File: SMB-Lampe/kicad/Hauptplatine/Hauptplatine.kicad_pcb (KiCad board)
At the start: 2 copper layers, 2 parts, among them J1 Screw_Terminal_01x03, U1 MOUDLE-SEEEDUINO-XIAO-ESP32C3

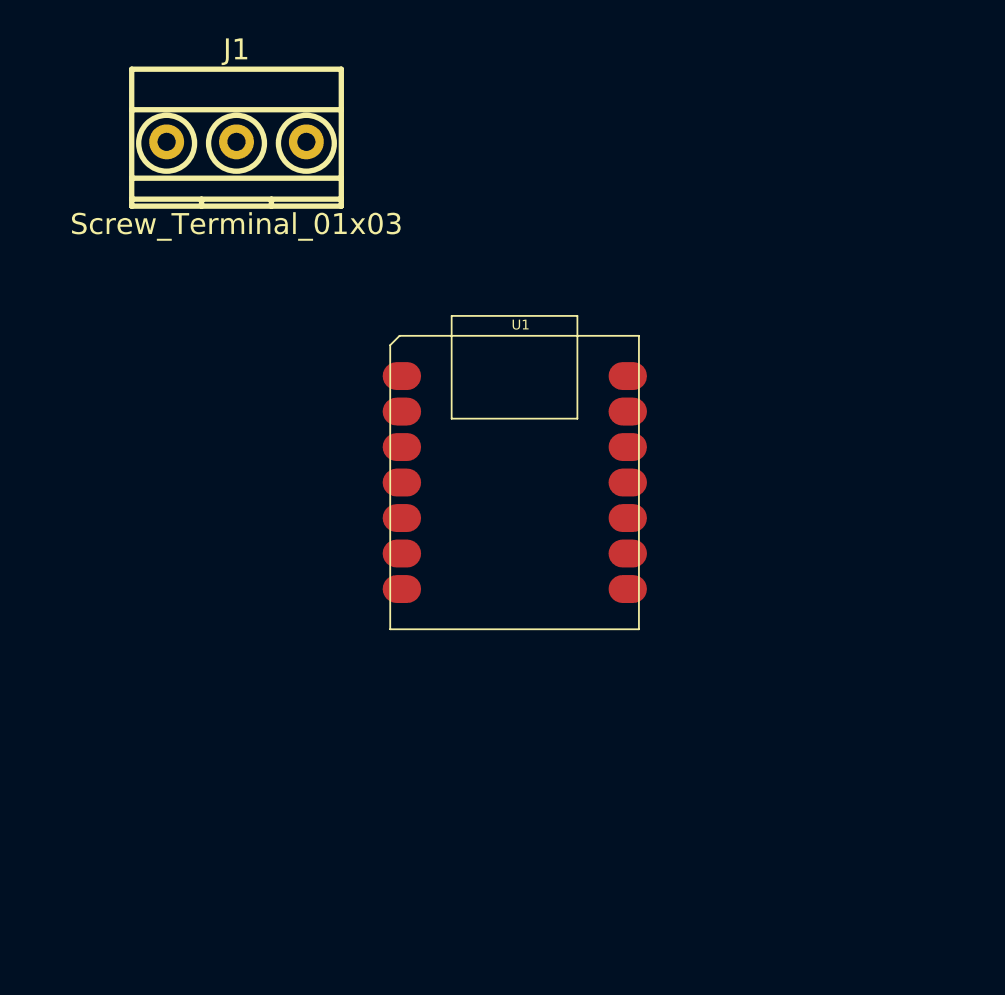
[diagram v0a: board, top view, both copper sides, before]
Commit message: Hauptplatine fertig
Hauptplatine mit ESP Levelshifter und Screwsockets
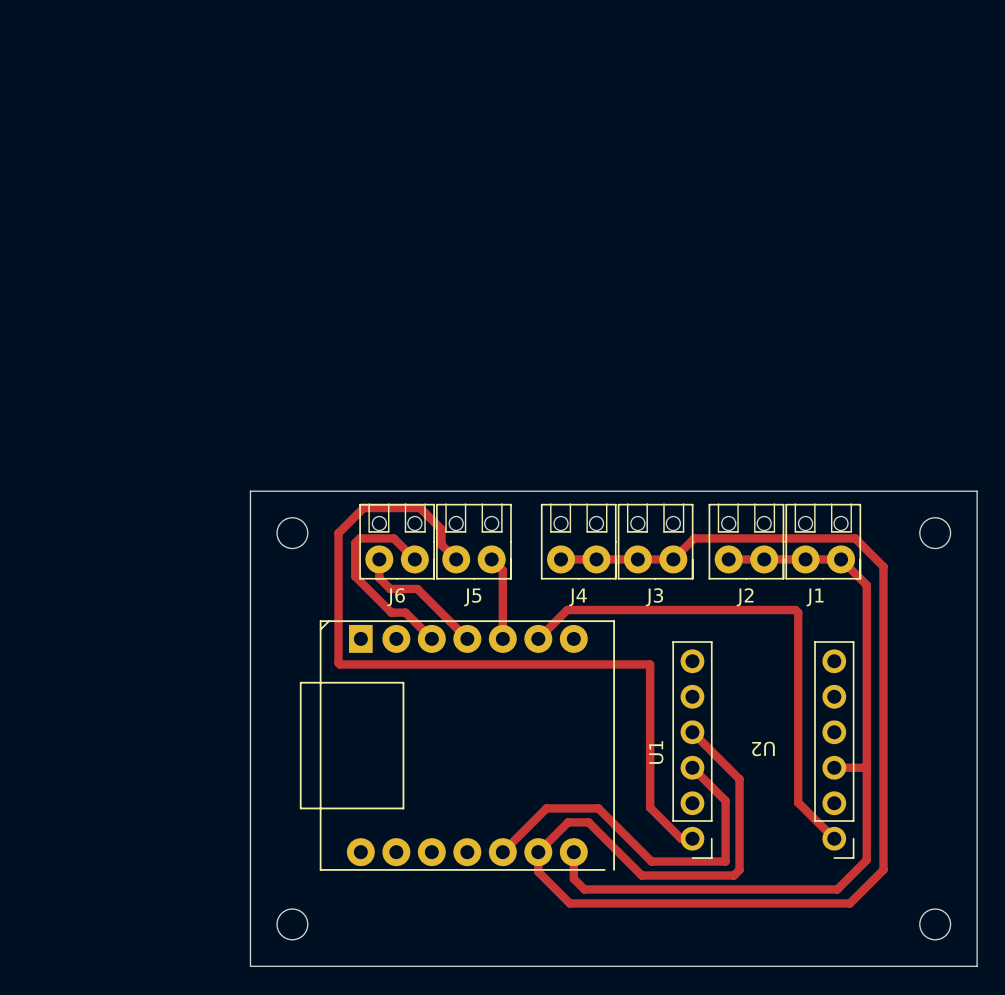
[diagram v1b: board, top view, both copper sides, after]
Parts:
- added J2: Screw_Terminal_01x02, Eigenen_Library:Screw Terminal, F.Cu at (141.5, 79.9)
- added J3: Screw_Terminal_01x02, Eigenen_Library:Screw Terminal, F.Cu at (135.0, 79.9)
- added J4: Screw_Terminal_01x02, Eigenen_Library:Screw Terminal, F.Cu at (129.5, 79.9)
- added J5: Screw_Terminal_01x02, Eigenen_Library:Screw Terminal, F.Cu at (122.0, 79.9)
- added J6: Screw_Terminal_01x02, Eigenen_Library:Screw Terminal, F.Cu at (116.5, 79.9)
- added REF**: MountingHole_2.2mm_M2_DIN965, MountingHole:MountingHole_2.2mm_M2_DIN965, F.Cu at (155.0, 110.0)
- added REF**: MountingHole_2.2mm_M2_DIN965, MountingHole:MountingHole_2.2mm_M2_DIN965, F.Cu at (155.0, 82.0)
- added REF**: MountingHole_2.2mm_M2_DIN965, MountingHole:MountingHole_2.2mm_M2_DIN965, F.Cu at (109.0, 110.0)
- added REF**: MountingHole_2.2mm_M2_DIN965, MountingHole:MountingHole_2.2mm_M2_DIN965, F.Cu at (109.0, 82.0)
- added U2: 4-Kanal-I2C Pegelwandler, Eigenen_Library:I2C Levelshifter, F.Cu at (142.8, 89.4)
- J1: value Screw_Terminal_01x03 -> Screw_Terminal_01x02; footprint w_conn_mkds:mkds_1,5-3 -> Eigenen_Library:Screw Terminal
- U1: footprint xiao ESP32C3_PCB:MOUDLE14P-SMD-2.54-21X17.8MM -> Eigenen_Library:ESP32 C3
- moved J1 49.3 mm to (147.0, 79.9), turned to 180 degrees
- moved U1 18.1 mm to (132.0, 97.2), turned to 90 degrees
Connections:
- J1 pad 1: unconnected-(J1-Pin_1-Pad1) -> +5V
- J1 pad 2: unconnected-(J1-Pin_2-Pad2) -> +5V
- U1 pad 12: unconnected-(U1-3V3-Pad12) -> +3.3V
- U1 pad 13: unconnected-(U1-GND-Pad13) -> GND
- U1 pad 14: unconnected-(U1-5V-Pad14) -> +5V
- U1 pad 3: unconnected-(U1-PA10_A2_D2-Pad3) -> Steuer_Servo
- U1 pad 4: unconnected-(U1-PA11_A3_D3-Pad4) -> Daten_LED
- U1 pad 5: unconnected-(U1-PA8_A4_D4_SDA-Pad5) -> /TRIG_Ultraschall
- U1 pad 6: unconnected-(U1-PA9_A5_D5_SCL-Pad6) -> Net-(U1-PA9_A5_D5_SCL)
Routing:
- net GND: track 0.00 -> 102.5 mm
- net /ECHO_Ultraschall: track 0.00 -> 57.2 mm
- net +5V: track 0.00 -> 56.7 mm
- net Net-(U1-PA9_A5_D5_SCL): track 0.00 -> 36.8 mm
- net +3.3V: track 0.00 -> 26.5 mm
- net Steuer_Servo: track 0.00 -> 14.7 mm
- net Daten_LED: track 0.00 -> 9.44 mm
- net /TRIG_Ultraschall: track 0.00 -> 6.02 mm
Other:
- board outline added: 52 x 34 mm

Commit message: Nachträgliche Änderungen für die Fertigung und Präsentation
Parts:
- U1: value MOUDLE-SEEEDUINO-XIAO-ESP32C3 -> ESP32C3 SEEED Studio
- moved REF** 1.12 mm to (154.5, 109.0)
- moved REF** 1.12 mm to (154.5, 81.0)
- moved REF** 1.12 mm to (108.5, 109.0)
- moved REF** 1.12 mm to (108.5, 81.0)
- moved U1 0.09 mm to (132.0, 97.1)
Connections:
- net Daten_LED renamed Data_LED
- U2 pad 10: unconnected-(U2-GND-Pad10) -> GND
- U2 pad 4: GND -> unconnected-(U2-GND-Pad4)
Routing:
- net GND: track 102.5 -> 122.0 mm
- net +5V: track 56.7 -> 71.9 mm
- net +3.3V: track 26.5 -> 33.7 mm
- net Net-(U1-PA9_A5_D5_SCL): track 36.8 -> 39.7 mm
- net /ECHO_Ultraschall: track 57.2 -> 58.6 mm
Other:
- board size 52 x 34 mm -> 50 x 32 mm
